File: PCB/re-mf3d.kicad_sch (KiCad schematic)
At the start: 43 parts, among them J1 USB_B, P1 Conn_02x05_Odd_Even, P2 Conn_01x06_Female, Q1 Q_NMOS_GSD, Q2 Q_NMOS_GSD, SW23 SW_Push, SW24 SW_Push, U10 ITG-3200, U7 MMA8453QR1, U8 ZXCL330H5TA, U9 ATmega32U4-A, X1 16MHz

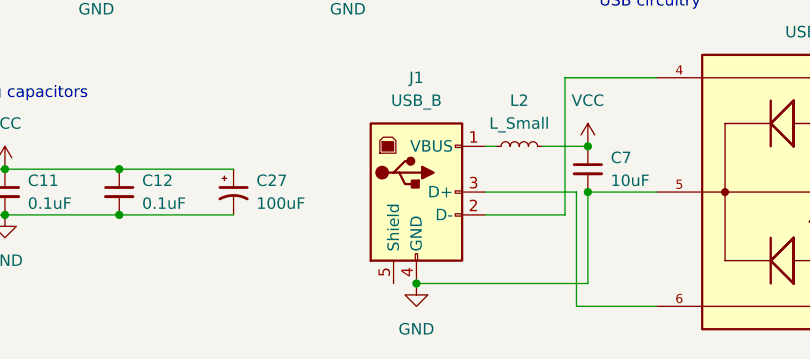
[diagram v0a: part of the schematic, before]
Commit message: Added some ground fills
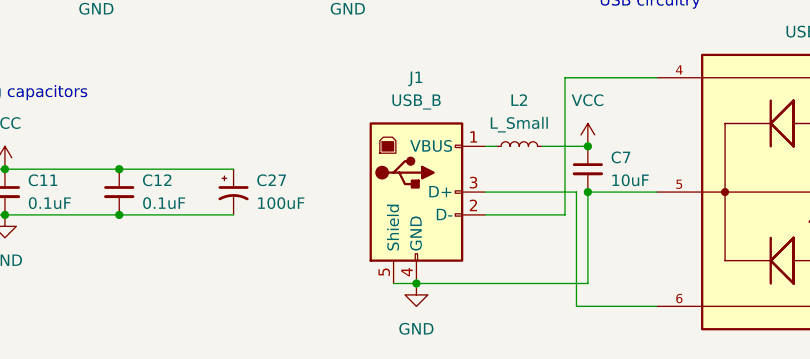
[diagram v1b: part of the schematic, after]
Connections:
- net GND: now also J1.5 (Shield)
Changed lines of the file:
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@@
+    (stroke (width 0) (type default) (color 0 0 0 0))
+  )
+  (wire (pts (xy 85.09 185.42) (xy 87.63 185.42))
     (stroke (width 0) (type default) (color 0 0 0 0))
   )

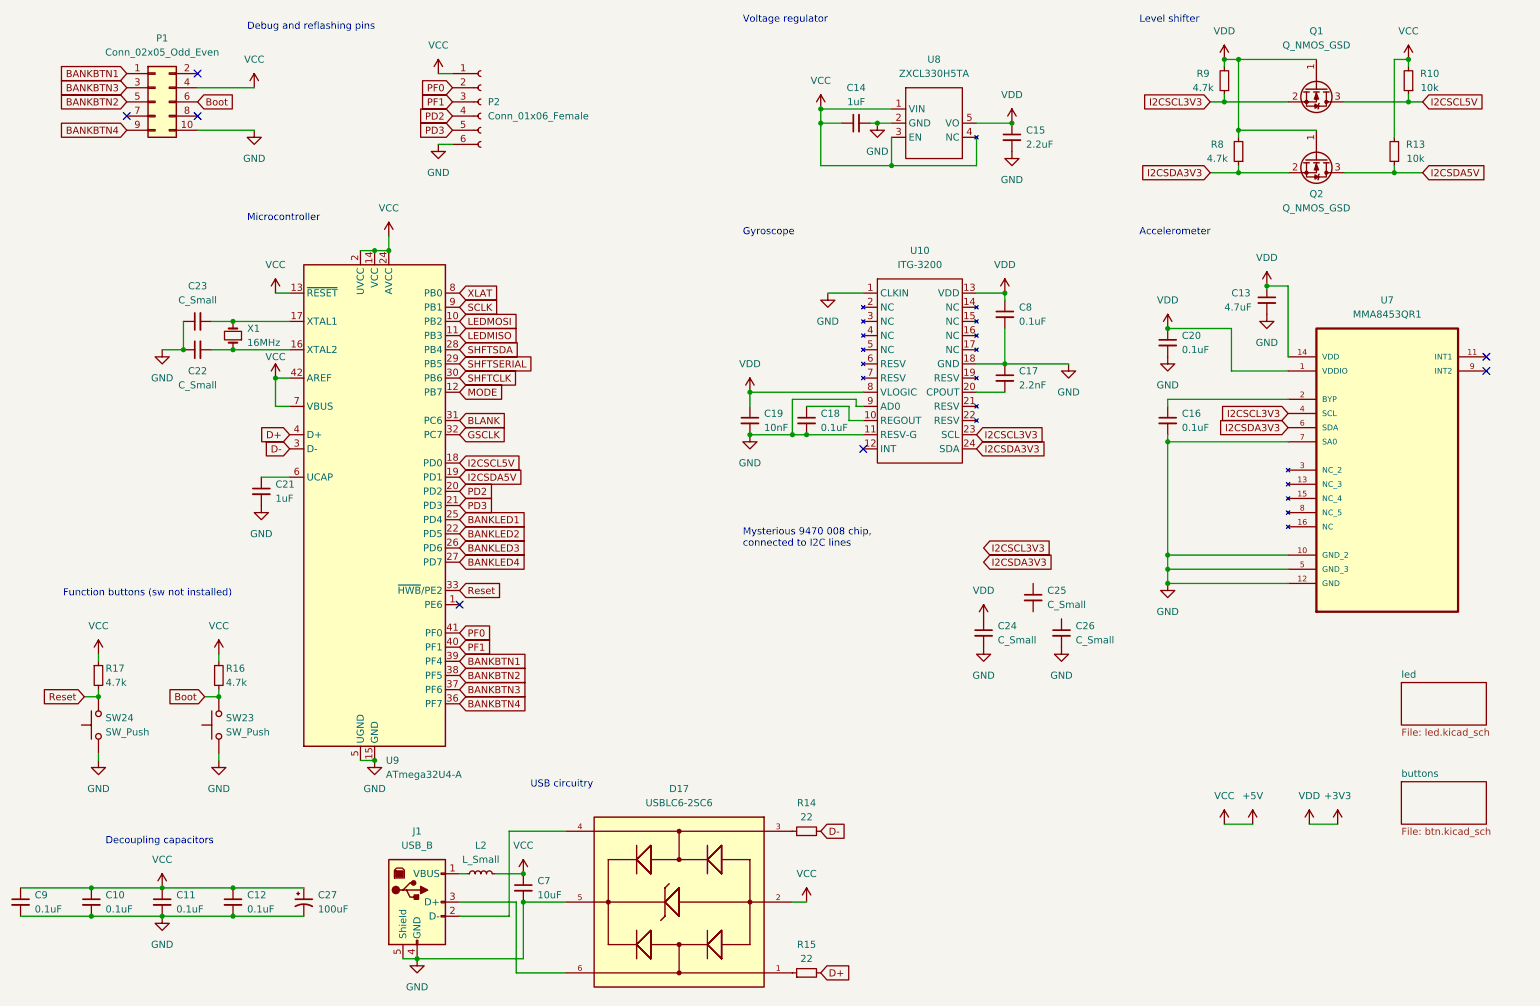
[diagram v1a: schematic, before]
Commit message: Migrate to kicad7 and component updates
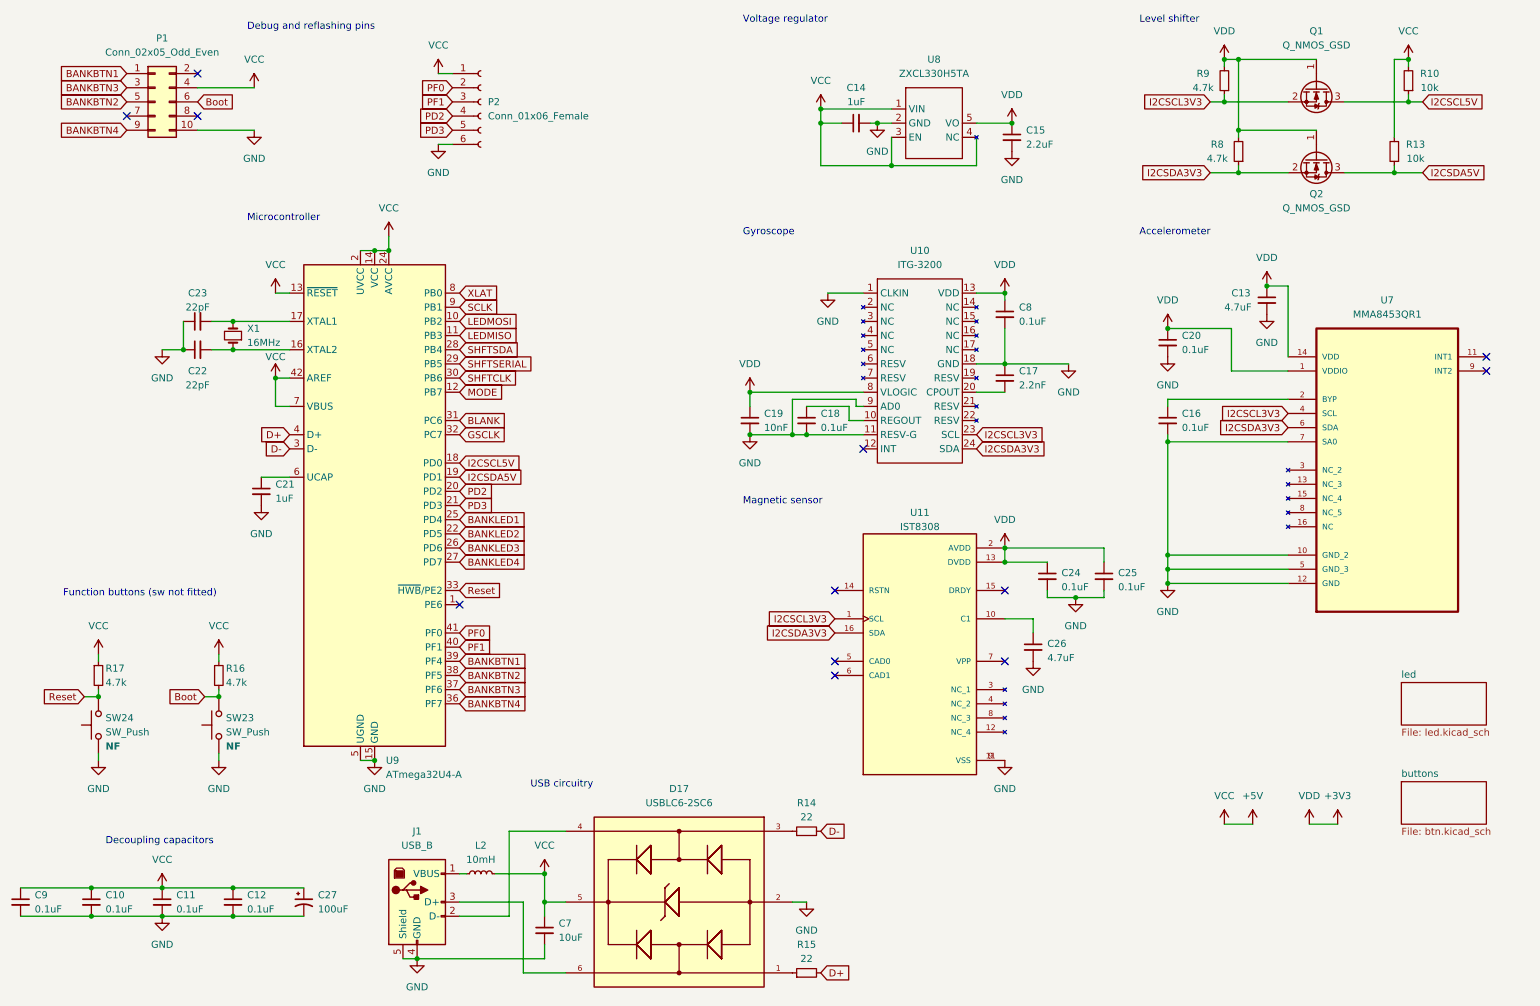
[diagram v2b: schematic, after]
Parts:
- added U11: IST8308, assets:PQFN50P300X300X110-16N, symbol assets:IST8308
- C22, C23: value C_Small -> 22pF
- C24, C25: value C_Small -> 0.1uF
- C26: value C_Small -> 4.7uF
- L2: value L_Small -> 10mH
- SW23, SW24: NotFitted (none) -> NF
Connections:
- net +3V3: now also C25.1, U11.13 (DVDD), U11.2 (AVDD)
- net +5V: now also D17.5; no longer D17.2
- net GND: now also C25.2, D17.2, U11.11 (VSS), U11.9 (VSS); no longer D17.5
- net I2CSCL3V3: now also U11.1 (SCL)
- net I2CSDA3V3: now also U11.16 (SDA)
- net at C26.1: now also U11.10 (C1)
- no-connect marks 7 -> 12
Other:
- note added: "Function buttons (sw not fitted)"
- note added: "Magnetic sensor"
- note removed: "Function buttons (sw not installed)"
- note removed: "Mysterious 9470 008 chip, connected to I2C lines"
- moved on the sheet: C24, C25, C26, C7
